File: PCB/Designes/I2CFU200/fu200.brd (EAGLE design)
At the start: 100 x 80 mm, 26 parts, among them IC2 LM358N, K1 FINDER-30.22, K2 FINDER-30.22, K3 FINDER-30.22, Q1 BS170, Q2 BS170, Q3 BS170, U1 ATMEGA328P-AU, X1 250-111, X2 250-111, X3 250-102

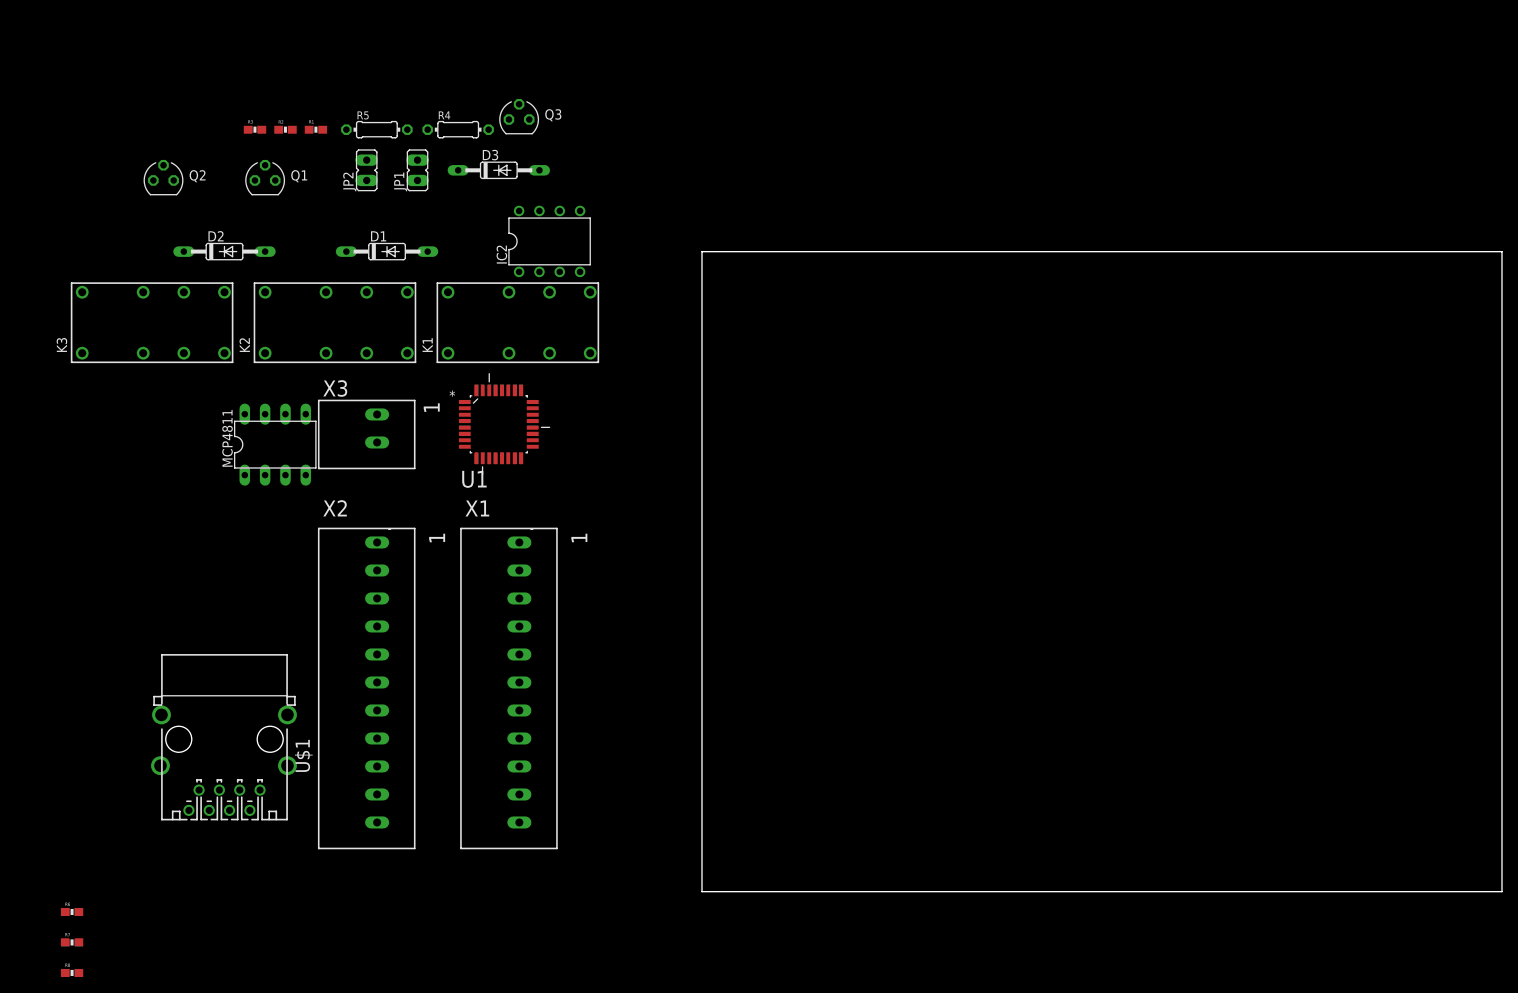
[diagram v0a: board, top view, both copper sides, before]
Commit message: FU200
Freuquenzumrichter als neues Device erstellt, Transistoren und wagt
klemmen hinzugefügt
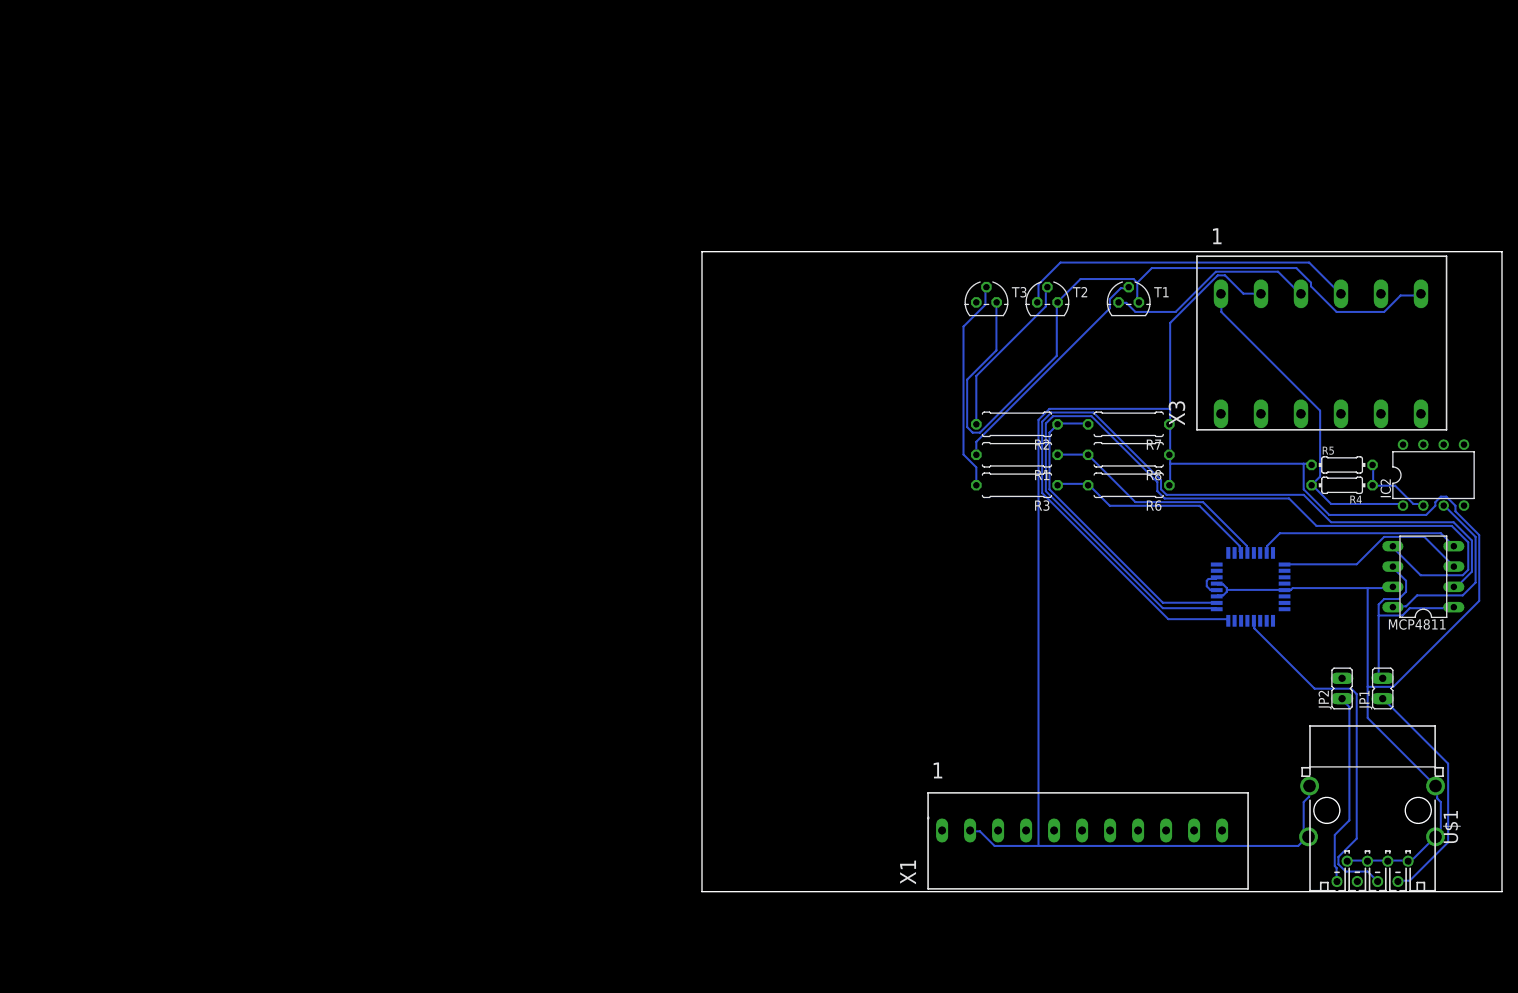
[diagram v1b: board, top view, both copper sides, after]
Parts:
- removed D1, D2, D3: 1N4148DO35-10, diode:DO35-10
- removed K1, K2, K3: FINDER-30.22, relay:FINDER-30.22
- removed Q1, Q2, Q3: BS170, transistor-small-signal:SOT54E
- removed X2: 250-111, con-wago_250:P-250-111
- added T1, T2, T3: 2N3565, transistor:TO92
- R1, R2, R3: value 100k -> 4,7k; device SparkFun-Resistors:0603-RES -> resistor:0309/10
- R6, R7, R8: value 100 -> (none); device SparkFun-Resistors:0603-RES -> resistor:0309/10
- X3: value 250-102 -> 250-706; device con-wago_250:P-250-102 -> con-wago_250:P-250-706
- moved R7 147.1 mm to (53.3, 58.4), turned to 180 degrees
- moved R8 147.1 mm to (53.3, 54.6), turned to 180 degrees
- moved MCP4811 144.5 mm to (90.2, 39.4), turned to 90 degrees
- moved U$1 143.8 mm to (83.8, 8.89)
- moved R6 142.4 mm to (53.3, 50.8), turned to 180 degrees
- moved JP2 138.1 mm to (80.0, 25.4)
- moved JP1 136.9 mm to (85.1, 25.4)
- moved R5 127.7 mm to (80.0, 53.3)
- moved X3 119.9 mm to (77.5, 68.6), turned to 90 degrees
- moved R4 119.1 mm to (80.0, 50.8), turned to 180 degrees
- moved IC2 114.3 mm to (91.4, 52.1)
- moved R3 105.1 mm to (39.4, 50.8), turned to 180 degrees
- moved R2 98.6 mm to (39.4, 58.4), turned to 180 degrees
- moved R1 96.6 mm to (39.4, 54.6), turned to 180 degrees
- moved U1 96.2 mm to (68.6, 38.1), flipped to the bottom, turned to 180 degrees
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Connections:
- removed net N$11: K1.22, X2.L1
- removed net N$14: K1.12, X1.L3
- removed net N$17: K1.14, X1.L5
- removed net N$18: K2.12, X1.L6
- removed net N$19: K2.11, X1.L7
- removed net N$20: K2.14, X1.L8
- removed net N$21: K3.12, X1.L9
- removed net N$22: K3.11, X1.L10
- removed net N$23: K3.14, X1.L11
- removed net N$24: K1.21, X2.L2
- removed net N$25: K1.24, X2.L3
- removed net N$26: K2.22, X2.L4
- removed net N$27: K2.21, X2.L5
- removed net N$28: K2.24, X2.L6
- removed net N$29: K3.22, X2.L7
- removed net N$3: R1.1, R8.1
- removed net N$30: K3.21, X2.L8
- removed net N$31: K3.24, X2.L9
- removed net N$36: Q1.G, R8.2
- removed net N$38: Q2.G, R7.2
- removed net N$40: IC2.1, R4.2, X3.L1
- removed net N$41: Q3.G, R6.2
- removed net N$8: D2.A, K2.A2, Q2.D
- removed net N$9: D3.A, K3.A2, Q3.D
- removed net VCC: U1.6
- new net 0-10V: IC2.1, R4.2, X3.L1.1
- new net DCM: T1.1, T2.1, T3.1, X3.L6.1
- new net FOR: T3.3, X3.L5.1
- new net GND: MCP4811.7, R5.1, R6.1, R7.1, R8.1, U$1.1_GND, U$1.3_GND, U$1.5_GND, U$1.7_GND, U$1.G1, U$1.G2, U$1.G3, U$1.G4, U1.21, U1.3, U1.5, X1.L2, X3.L2.1
- new net REV: T2.3, X3.L4.1
- new net RST: T1.3, X3.L3.1
- net N$1: now also R1.1, R8.2, U1.12; no longer D1.A, K1.A2, Q1.D
- net N$12: now also R7.2; no longer R7.1
- net N$13: now also JP1.2, MCP4811.1, MCP4811.6, U1.4, U1.6, X1.L1; no longer MCP4811.7, Q1.S, Q2.S, Q3.S, R1.2, R2.2, R3.2, R5.1, U$1.1_GND, U$1.3_GND, U$1.5_GND, U$1.7_GND, U$1.G1, U$1.G2, U$1.G3, U$1.G4, U1.21, U1.3, U1.5, X3.L2
- net N$15: now also R6.2; no longer R6.1
- net N$16: now also R2.2, T2.2; no longer K1.11, X1.L4
- net N$2: now also R1.2, T1.2; no longer JP1.2, MCP4811.1, MCP4811.6, U1.4
- net N$5: now also R3.2, T3.2; no longer D1.C, D2.C, D3.C, K1.A1, K2.A1, K3.A1
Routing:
- net GND: track 0.00 -> 302.8 mm
- net N$37: track 0.00 -> 111.0 mm
- net N$32: track 0.00 -> 107.3 mm
- net DCM: track 0.00 -> 93.0 mm
- net N$6: track 0.00 -> 45.2 mm
- net REV: track 0.00 -> 42.8 mm
- net 0-10V: track 0.00 -> 42.0 mm
- net N$12: track 0.00 -> 39.2 mm
- net N$13: track 0.00 -> 30.8 mm
- net N$10: track 0.00 -> 29.7 mm
- net N$2: track 0.00 -> 29.4 mm
- net N$1: track 0.00 -> 29.3 mm
- net N$15: track 0.00 -> 27.1 mm
- net N$5: track 0.00 -> 26.6 mm
- net RST: track 0.00 -> 26.5 mm
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
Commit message: ++
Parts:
- removed X1: 250-111, con-wago_250:P-250-111
- added D1, D2: 1N4148DO35-7, diode:DO35-7
- added OK1, OK2: CNY17, optocoupler:DIL06
- added R10, R11: 4,7kOhm, resistor:0204/7
- added R9: 1,2kOhm, resistor:0204/7
- added U$2: HUN_FU2, Btz:HUN_FU2
- added U2: ATMEGA328P-AU, Atmel-ATMEGA328P-AU:QFP80P900X900X120-32N
- added X2: 250-706, con-wago_250:P-250-706
- added X4: 250-704, con-wago_250:P-250-704
- R6, R7: value (none) -> R10K
- R8: value (none) -> 1,2kOhm; device resistor:0309/10 -> resistor:0204/7
- moved IC2 164.3 mm to (-71.1, 76.2)
- moved R5 155.8 mm to (-68.6, 100.3)
- moved MCP4811 153.4 mm to (-58.4, 77.5), turned to 0 degrees
- moved JP2 151.7 mm to (-57.1, 90.2)
- moved JP1 150.5 mm to (-50.8, 90.2)
- moved R4 147.0 mm to (-58.4, 100.3), turned to 0 degrees
- moved U$1 144.2 mm to (-52.1, 57.1)
- moved R8 139.8 mm to (-78.7, 100.3), turned to 0 degrees
- moved R2 123.2 mm to (-80.0, 88.9), turned to 0 degrees
- moved T2 120.1 mm to (-74.9, 95.2)
- moved T1 116.3 mm to (-61.0, 95.2)
- moved R1 112.1 mm to (-67.3, 88.9), turned to 0 degrees
- moved R7 104.5 mm to (-44.5, 95.2), turned to 0 degrees
- moved R6 96.0 mm to (-31.8, 95.2), turned to 0 degrees
- moved R3 73.4 mm to (-19.1, 95.2), turned to 0 degrees
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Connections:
- removed net DCM: T1.1, T2.1, T3.1, X3.L6.1
- removed net RST: T1.3, X3.L3.1
- new net +12V: X2.L1.2, X3.L1.1, X3.L3.1, X3.L5.1
- new net +5V: JP1.2, MCP4811.1, MCP4811.6, U1.4, U1.6, X3.L1.2, X3.L4.2, X3.L6.2, X4.L1.1, X4.L1.2
- new net DIR: X2.L5.2
- new net EN: X2.L4.2
- new net N$11: U$2.P$14
- new net N$17: U$2.P$1
- new net N$18: D1.C, OK1.1
- new net N$19: D2.C, OK2.1
- new net N$20: R9.2
- new net N$21: R10.1, R11.1
- new net N$22: OK2.5, R11.2
- new net N$23: R9.1, X3.L4.1
- new net N$24: R8.1, X3.L6.1
- new net N$25: OK1.5, R10.2
- new net N$3: U$2.P$5
- new net N$8: U$2.P$15
- new net N$9: U$2.P$6
- new net PUL: X2.L3.2
- new net RES: T1.1, X2.L3.1
- new net TEMP1: R6.2, U1.23, X3.L3.2
- new net TEMP2: R7.2, X3.L5.2
- new net VCC: U2.6
- new net VCC_2: U2.4
- net 0-10V: now also X2.L1.1; no longer X3.L1.1
- net AVCC: now also U2.18
- net FOR: now also T3.1, X2.L5.1; no longer T3.3, X3.L5.1
- net GND: now also D1.A, D2.A, OK1.2, OK1.4, OK2.2, OK2.4, T1.3, T2.3, T3.3, U2.3, U2.5, X2.L2.1, X2.L2.2, X2.L6.1, X2.L6.2, X3.L2.2, X4.L4.1, X4.L4.2; no longer R8.1, X1.L2
- net N$1: no longer R1.1, R8.2
- net N$12: no longer R7.2
- net N$13: now also R8.2; no longer JP1.2, MCP4811.1, MCP4811.6, U1.4, U1.6, X1.L1
- net N$15: no longer R6.2
- net N$32: no longer U1.32
- net N$37: no longer U1.1
- net REV: now also T2.1, X2.L4.1; no longer T2.3, X3.L4.1
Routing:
- net GND: track 302.8 -> 0.00 mm
- net N$37: track 111.0 -> 0.00 mm
- net N$32: track 107.3 -> 0.00 mm
- net DCM: track 93.0 -> 0.00 mm
- net N$6: track 45.2 -> 0.00 mm
- net REV: track 42.8 -> 0.00 mm
- net 0-10V: track 42.0 -> 0.00 mm
- net N$12: track 39.2 -> 0.00 mm
- net N$13: track 30.8 -> 0.00 mm
- net N$10: track 29.7 -> 0.00 mm
- net N$2: track 29.4 -> 0.00 mm
- net N$1: track 29.3 -> 0.00 mm
- net N$15: track 27.1 -> 0.00 mm
- net N$5: track 26.6 -> 0.00 mm
- net RST: track 26.5 -> 0.00 mm
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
